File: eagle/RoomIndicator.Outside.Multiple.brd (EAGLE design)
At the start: 112 x 104 mm, 124 parts, among them IC1 MEGA328P, IC2 MEGA328P, IC3 MEGA328P, IC4 MEGA328P, Q1 8MHz, Q2 8MHz, Q3 8MHz, Q4 8MHz, T1 BC847, T10 BC847, T11 BC847, T12 BC847, T2 BC847, T3 BC847, T4 BC847, T5 BC847, T6 BC847, T7 BC847, T8 BC847, T9 BC847, U1 3.3V/150mA, U2 3.3V/150mA, U3 3.3V/150mA, U4 3.3V/150mA

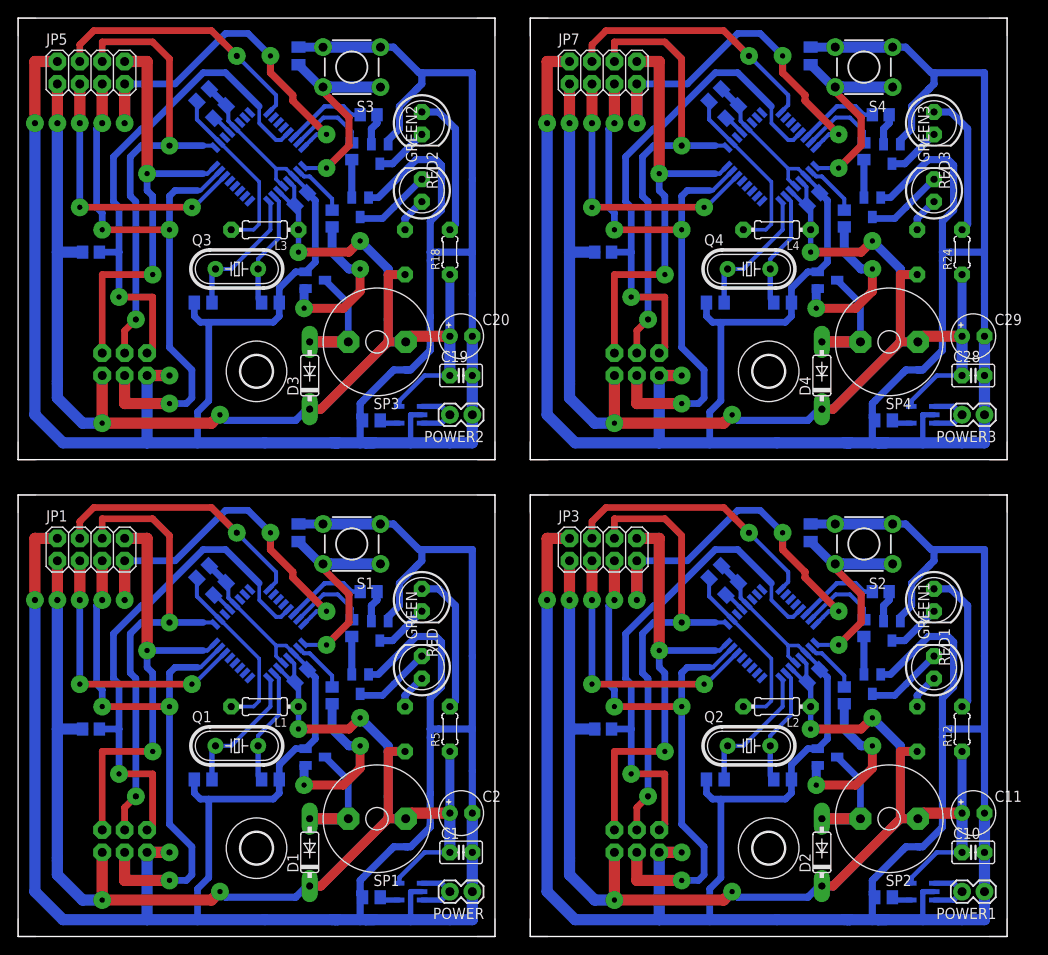
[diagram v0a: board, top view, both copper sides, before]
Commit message: Replacing buzzer package
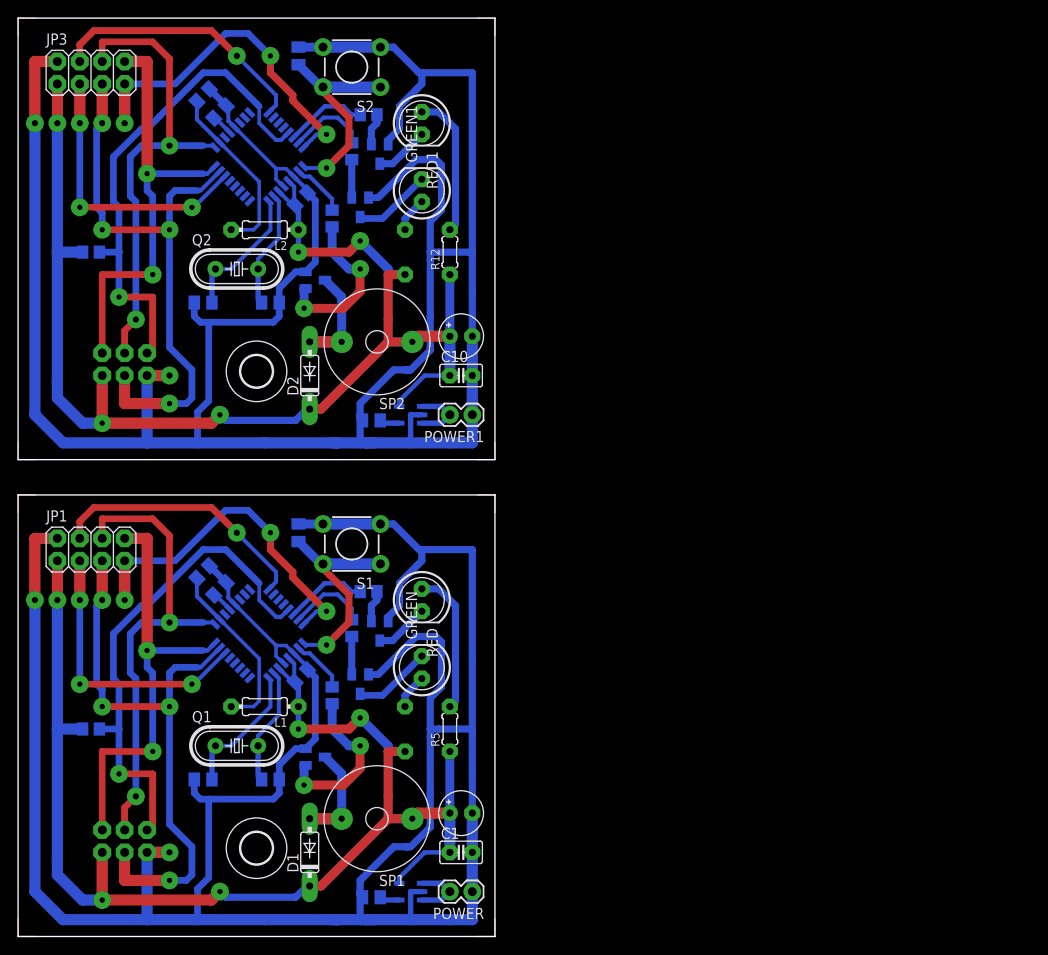
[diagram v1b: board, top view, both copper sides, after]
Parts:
- removed C19, C28: 100n, rcl:C025-025X050
- removed C20, C29: 100uF, rcl:E2,5-5
- removed C21, C22, C23, C26, C30, C31, C32, C35: 100n, rcl:C0805K
- removed C24, C25, C33, C34: 27p, rcl:C0805K
- removed C27, C36: 180p, rcl:C0805K
- removed D3, D4: 1N4148, diode:DO35-7
- removed GREEN2, GREEN3, RED2, RED3: GREEN, led:LED5MM
- removed IC3, IC4: MEGA328P, atmel:TQFP32-08
- removed JP5, JP7: NRF24L01, pinhead:2X04
- removed JP6, JP8: SPI, SparkFun-Connectors:2X3
- removed L3, L4: 10uH, rcl:0204/7
- removed POWER2, POWER3: (no value), SparkFun-Connectors:1X02
- removed Q3, Q4: 8MHz, crystal:HC49/S
- removed R13, R14, R16, R17, R19, R20, R22, R23: 10k, rcl:R0805
- removed R15, R18, R21, R24: 30, rcl:0204/5
- removed S3, S4: (no value), SparkFun-Retired:TACTILE-PTH
- removed SP3, SP4: AL60P, buzzer:AL60P
- removed T10, T11, T12, T7, T8, T9: BC847, transistor:SOT23
- removed U$3, U$4: (no value), holes:3,6
- removed U3, U4: 3.3V/150mA, SparkFun-PowerIC:SOT23-5
- SP1, SP2: value AL60P -> AL60PWIDE; device buzzer:AL60P -> buzzer:AL80P
- moved C10 79.2 mm to (50.2, 63.5)
- moved C11 79.2 mm to (50.2, 68.0)
- moved C13 79.2 mm to (22.9, 93.4)
- moved C14 79.2 mm to (21.0, 95.3)
- moved IC2 79.2 mm to (27.3, 88.3)
- moved JP4 79.2 mm to (9.53, 66.1)
- moved R10 79.2 mm to (35.6, 81.3)
- moved C12 79.2 mm to (32.1, 83.5)
- moved C15 79.2 mm to (28.6, 71.8)
- moved C16 79.2 mm to (21.0, 71.8)
- moved C17 79.2 mm to (31.8, 99.7)
- moved C18 79.2 mm to (40.0, 58.4)
- moved D2 79.2 mm to (33.0, 63.5)
- moved GREEN1 79.2 mm to (45.7, 84.5)
- moved JP3 79.2 mm to (8.26, 97.8)
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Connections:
- removed net +3V2: C19.1, C20.+, C21.2, D3.C, IC3.4, IC3.6, JP5.1, JP6.2, L3.1, R13.2, R15.1, R18.1, SP3.1, U3.5
- removed net +3V4: C28.1, C29.+, C30.2, D4.C, IC4.4, IC4.6, JP7.1, JP8.2, L4.1, R19.2, R21.1, R24.1, SP4.1, U4.5
- removed net AVCC2: C23.1, IC3.18, L3.2
- removed net AVCC3: C32.1, IC4.18, L4.2
- removed net BLUE2: IC3.31, R14.2
- removed net BLUE3: IC4.31, R20.2
- removed net BUZZ2: IC3.2, R16.1
- removed net BUZZ3: IC4.2, R22.1
- removed net CE2: IC3.25, JP5.4
- removed net CE3: IC4.25, JP7.4
- removed net CSN2: IC3.14, JP5.3
- removed net CSN3: IC4.14, JP7.3
- removed net GND2: C19.2, C20.-, C21.1, C22.1, C23.2, C24.1, C25.1, C26.1, C27.2, IC3.21, IC3.3, IC3.5, JP5.2, JP6.6, POWER2.1, S3.3, S3.4, T7.2, T8.2, T9.2, U3.2
- removed net GND3: C28.2, C29.-, C30.1, C31.1, C32.2, C33.1, C34.1, C35.1, C36.2, IC4.21, IC4.3, IC4.5, JP7.2, JP8.6, POWER3.1, S4.3, S4.4, T10.2, T11.2, T12.2, U4.2
- removed net INT4: C26.2, IC3.1, S3.1, S3.2
- removed net INT5: IC3.32, JP5.7
- removed net INT6: C35.2, IC4.1, S4.1, S4.2
- removed net INT7: IC4.32, JP7.7
- removed net MISO2: IC3.16, JP5.8, JP6.1
- removed net MISO3: IC4.16, JP7.8, JP8.1
- removed net MOSI2: IC3.15, JP5.5, JP6.4
- removed net MOSI3: IC4.15, JP7.5, JP8.4
- removed net N$39: C22.2, IC3.20
- removed net N$40: R14.1, T7.1
- removed net N$41: GREEN2.K, T7.3
- removed net N$42: D3.A, SP3.2, T8.3
- removed net N$43: R16.2, T8.1
- removed net N$44: GREEN2.A, R15.2
- removed net N$45: POWER2.2, U3.1, U3.3
- removed net N$46: R17.1, T9.1
- removed net N$47: RED2.K, T9.3
- removed net N$48: R18.2, RED2.A
- removed net N$49: C27.1, U3.4
- removed net N$58: C31.2, IC4.20
- removed net N$59: R20.1, T10.1
- removed net N$60: GREEN3.K, T10.3
- removed net N$61: D4.A, SP4.2, T11.3
- removed net N$62: R22.2, T11.1
- removed net N$63: GREEN3.A, R21.2
- removed net N$64: POWER3.2, U4.1, U4.3
- removed net N$65: R23.1, T12.1
- removed net N$66: RED3.K, T12.3
- removed net N$67: R24.2, RED3.A
- removed net N$68: C36.1, U4.4
- removed net RED2: IC3.30, R17.2
- removed net RED3: IC4.30, R23.2
- removed net RST2: IC3.29, JP6.5, R13.1
- removed net RST3: IC4.29, JP8.5, R19.1
- removed net SCK2: IC3.17, JP5.6, JP6.3
- removed net SCK3: IC4.17, JP7.6, JP8.3
- removed net TOSC5: C25.2, IC3.8, Q3.1
- removed net TOSC6: C24.2, IC3.7, Q3.2
- removed net TOSC7: C34.2, IC4.8, Q4.1
- removed net TOSC8: C33.2, IC4.7, Q4.2
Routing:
- net GND3: track 299.6 -> 0.00 mm, vias 2 -> 0
- net GND2: track 299.6 -> 0.00 mm, vias 2 -> 0
- net +3V4: track 169.7 -> 0.00 mm, vias 5 -> 0
- net +3V2: track 169.7 -> 0.00 mm, vias 5 -> 0
- net MOSI3: track 66.5 -> 0.00 mm, vias 4 -> 0
- net MOSI2: track 66.5 -> 0.00 mm, vias 4 -> 0
- net RST3: track 57.2 -> 0.00 mm, vias 1 -> 0
- net RST2: track 57.2 -> 0.00 mm, vias 1 -> 0
- net SCK2: track 53.7 -> 0.00 mm, vias 2 -> 0
- net SCK3: track 53.7 -> 0.00 mm, vias 2 -> 0
- net MISO2: track 49.6 -> 0.00 mm, vias 2 -> 0
- net MISO3: track 49.6 -> 0.00 mm, vias 2 -> 0
- net INT5: track 43.6 -> 0.00 mm, vias 3 -> 0
- net INT7: track 43.6 -> 0.00 mm, vias 3 -> 0
- net CSN3: track 31.9 -> 0.00 mm, vias 3 -> 0
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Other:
- board size 112 x 104 mm -> 54 x 104 mm
